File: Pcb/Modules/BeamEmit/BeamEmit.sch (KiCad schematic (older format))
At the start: 15 parts, among them J1 MICRO_USB, Q1 Q_NMOS_GSD, U1 LM555N

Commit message: Update module pcbs
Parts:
- added X1, X2, X3, X4: HOLE, Mounting_Holes:MountingHole_2.5mm_Pad, symbol HOLE
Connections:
- no-connect marks 1 -> 4
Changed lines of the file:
@@
 	7050 4850 7050 5000
 $Comp
-L GND #PWR11
+L GND #PWR01
 U 1 1 59FD7258
 P 7050 5000
-F 0 "#PWR11" H 7050 4750 50  0001 C CNN
+F 0 "#PWR01" H 7050 4750 50  0001 C CNN
 F 1 "GND" H 7050 4850 50  0000 C CNN
 F 2 "" H 7050 5000 50  0000 C CNN
@@
 $EndComp
 $Comp
-L +5V #PWR1
+L +5V #PWR02
 U 1 1 5A21CEBB
 P 3100 4000
-F 0 "#PWR1" H 3100 3850 50  0001 C CNN
+F 0 "#PWR02" H 3100 3850 50  0001 C CNN
 F 1 "+5V" H 3100 4140 50  0000 C CNN
 F 2 "" H 3100 4000 50  0000 C CNN
@@
 $EndComp
 $Comp
-L GND #PWR2
+L GND #PWR03
 U 1 1 5A21D01D
 P 3100 4500
-F 0 "#PWR2" H 3100 4250 50  0001 C CNN
+F 0 "#PWR03" H 3100 4250 50  0001 C CNN
 F 1 "GND" H 3100 4350 50  0000 C CNN
 F 2 "" H 3100 4500 50  0000 C CNN
@@
 $EndComp
 $Comp
-L VCC #PWR3
+L VCC #PWR04
 U 1 1 5A21E1C2
 P 3300 4000
-F 0 "#PWR3" H 3300 3850 50  0001 C CNN
+F 0 "#PWR04" H 3300 3850 50  0001 C CNN
 F 1 "VCC" H 3300 4150 50  0000 C CNN
 F 2 "" H 3300 4000 50  0000 C CNN
@@
 	4700 4200 4850 4200
 $Comp
-L +5V #PWR6
+L +5V #PWR05
 U 1 1 5A21EBAD
 P 4700 4200
-F 0 "#PWR6" H 4700 4050 50  0001 C CNN
+F 0 "#PWR05" H 4700 4050 50  0001 C CNN
 F 1 "+5V" H 4700 4340 50  0000 C CNN
 F 2 "" H 4700 4200 50  0000 C CNN
@@
 $EndComp
 $Comp
-L GND #PWR4
+L GND #PWR06
 U 1 1 5A21EE4C
 P 4400 4350
-F 0 "#PWR4" H 4400 4100 50  0001 C CNN
+F 0 "#PWR06" H 4400 4100 50  0001 C CNN
 F 1 "GND" H 4400 4200 50  0000 C CNN
 F 2 "" H 4400 4350 50  0000 C CNN
@@
 Connection ~ 5550 4700
 $Comp
-L GND #PWR7
+L GND #PWR07
 U 1 1 5A21F0BA
 P 5550 5000
-F 0 "#PWR7" H 5550 4750 50  0001 C CNN
+F 0 "#PWR07" H 5550 4750 50  0001 C CNN
 F 1 "GND" H 5550 4850 50  0000 C CNN
 F 2 "" H 5550 5000 50  0000 C CNN
@@
 	4400 4000 4850 4000
 $Comp
-L +5V #PWR5
+L +5V #PWR08
 U 1 1 5A21F5D3
 P 4550 3400
-F 0 "#PWR5" H 4550 3250 50  0001 C CNN
+F 0 "#PWR08" H 4550 3250 50  0001 C CNN
 F 1 "+5V" H 4550 3540 50  0000 C CNN
 F 2 "" H 4550 3400 50  0000 C CNN
@@
 $EndComp
 $Comp
-L +5V #PWR8
+L +5V #PWR09
 U 1 1 5A21FBAE
 P 6100 3150
-F 0 "#PWR8" H 6100 3000 50  0001 C CNN
+F 0 "#PWR09" H 6100 3000 50  0001 C CNN
 F 1 "+5V" H 6100 3290 50  0000 C CNN
 F 2 "" H 6100 3150 50  0000 C CNN
@@
 $EndComp
 $Comp
-L GND #PWR9
+L GND #PWR010
 U 1 1 5A21FBE3
 P 6100 3350
-F 0 "#PWR9" H 6100 3100 50  0001 C CNN
+F 0 "#PWR010" H 6100 3100 50  0001 C CNN
 F 1 "GND" H 6100 3200 50  0000 C CNN
 F 2 "" H 6100 3350 50  0000 C CNN
@@
 $EndComp
 $Comp
-L +5V #PWR10
+L +5V #PWR011
 U 1 1 5A220329
 P 7050 3400
-F 0 "#PWR10" H 7050 3250 50  0001 C CNN
+F 0 "#PWR011" H 7050 3250 50  0001 C CNN
 F 1 "+5V" H 7050 3540 50  0000 C CNN
 F 2 "" H 7050 3400 50  0000 C CNN
@@
 Text Notes 4300 2800 0    60   ~ 0
 f = 1 / (0.693 * (2*(R3+R5) * C4)
+$Comp
+L HOLE X1
+U 1 1 5A22D73E
+P 4050 5500
+F 0 "X1" H 4050 5400 60  0000 C CNN
+F 1 "HOLE" H 4050 5600 60  0000 C CNN
+F 2 "Mounting_Holes:MountingHole_2.5mm_Pad" H 4050 5500 60  0001 C CNN
+F 3 "" H 4050 5500 60  0000 C CNN
+	1    4050 5500
+	1    0    0    -1
+$EndComp
+$Comp
+L HOLE X2
+U 1 1 5A22E2CB
+P 4350 5500
+F 0 "X2" H 4350 5400 60  0000 C CNN
+F 1 "HOLE" H 4350 5600 60  0000 C CNN
+F 2 "Mounting_Holes:MountingHole_2.5mm_Pad" H 4350 5500 60  0001 C CNN
+F 3 "" H 4350 5500 60  0000 C CNN
+	1    4350 5500
+	1    0    0    -1
+$EndComp
+$Comp
+L HOLE X3
+U 1 1 5A22E316
+P 4650 5500
+F 0 "X3" H 4650 5400 60  0000 C CNN
+F 1 "HOLE" H 4650 5600 60  0000 C CNN
+F 2 "Mounting_Holes:MountingHole_2.5mm_Pad" H 4650 5500 60  0001 C CNN
+F 3 "" H 4650 5500 60  0000 C CNN
+	1    4650 5500
+	1    0    0    -1
+$EndComp
+$Comp
+L HOLE X4
+U 1 1 5A22E364
+P 4950 5500
+F 0 "X4" H 4950 5400 60  0000 C CNN
+F 1 "HOLE" H 4950 5600 60  0000 C CNN
+F 2 "Mounting_Holes:MountingHole_2.5mm_Pad" H 4950 5500 60  0001 C CNN
+F 3 "" H 4950 5500 60  0000 C CNN
+	1    4950 5500
+	1    0    0    -1
+$EndComp
+NoConn ~ 2900 4150
+NoConn ~ 2900 4250
+NoConn ~ 2900 4350
 $EndSCHEMATC

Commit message: Update beam emitter to use single 20k
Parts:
- removed R5: 10K, Resistors_SMD:R_0603, symbol R
- R3: value 10K -> 20K
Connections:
- net at R4.1, U1.3 (Q): now also R3.2
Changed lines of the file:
@@
 P 5150 3400
 F 0 "R3" V 5230 3400 50  0000 C CNN
-F 1 "10K" V 5150 3400 50  0000 C CNN
+F 1 "20K" V 5150 3400 50  0000 C CNN
 F 2 "Resistors_SMD:R_0603" V 5080 3400 50  0001 C CNN
 F 3 "" H 5150 3400 50  0001 C CNN
 	1    5150 3400
-	0    -1   -1   0
-$EndComp
-$Comp
-L R R5
-U 1 1 5A21E86F
-P 5650 3400
-F 0 "R5" V 5730 3400 50  0000 C CNN
-F 1 "10K" V 5650 3400 50  0000 C CNN
-F 2 "Resistors_SMD:R_0603" V 5580 3400 50  0001 C CNN
-F 3 "" H 5650 3400 50  0001 C CNN
-	1    5650 3400
 	0    -1   -1   0
 $EndComp
@@
 	4800 3400 5000 3400
 Wire Wire Line
-	5800 3400 5900 3400
+	5300 3400 5900 3400
 Wire Wire Line
 	5900 3400 5900 3800
 Wire Wire Line
-	5500 3400 5300 3400
-Wire Wire Line
 	4700 4200 4850 4200

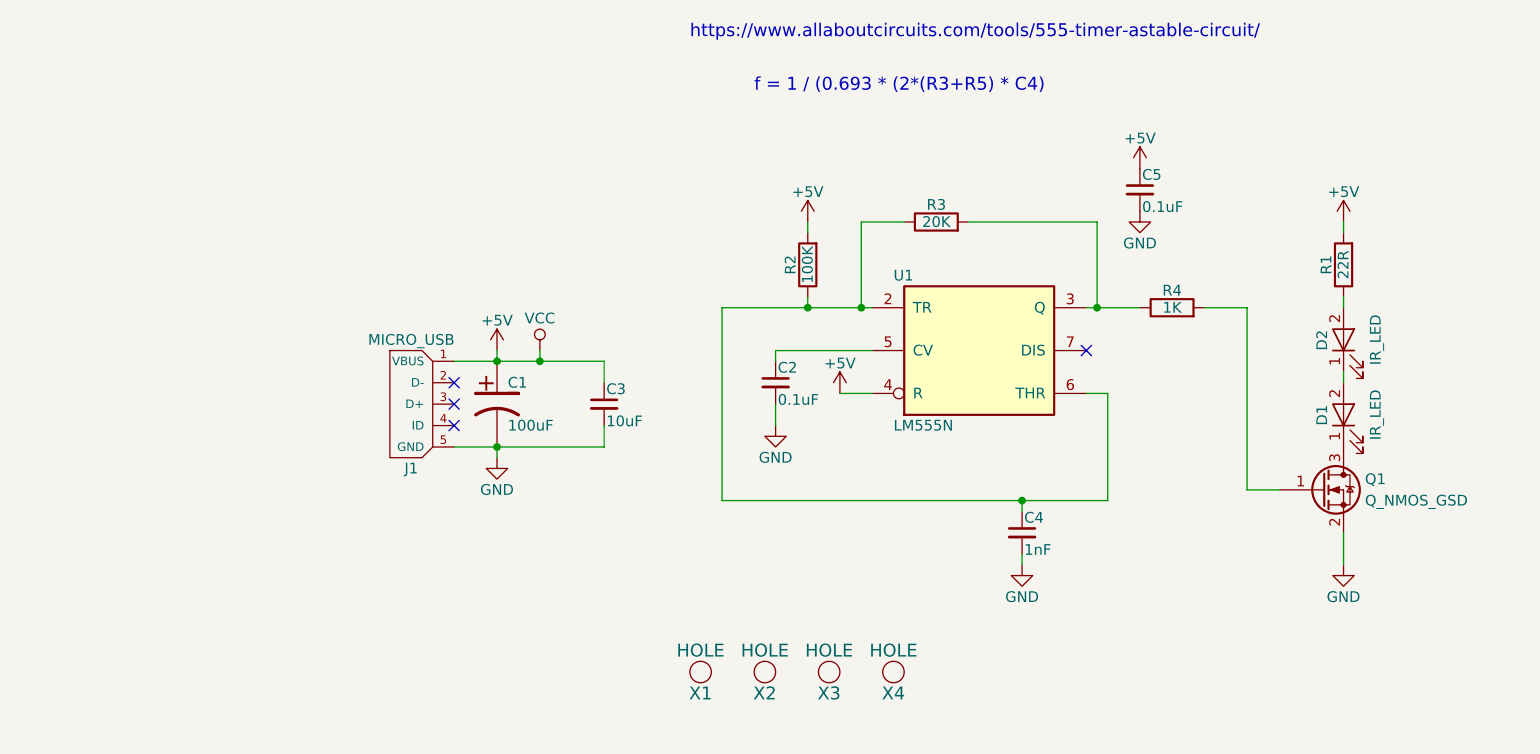
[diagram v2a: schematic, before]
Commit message: Update module pcbs
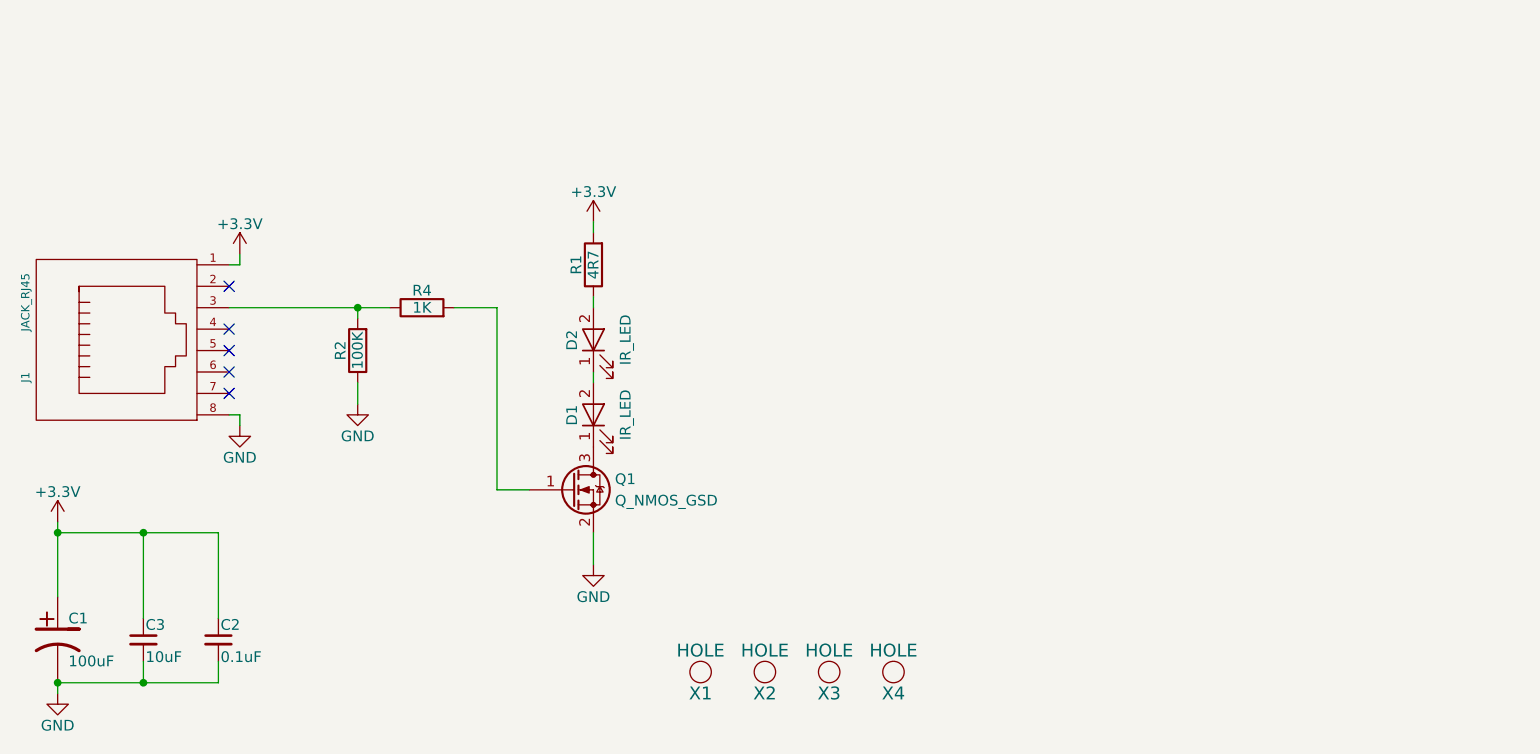
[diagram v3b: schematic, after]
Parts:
- removed C4: 1nF, Capacitors_SMD:C_0603, symbol C_Small
- removed C5: 0.1uF, Capacitors_SMD:C_0603, symbol C_Small
- removed J1: MICRO_USB, CA6:USB_MICRO_10118194-0001LF, symbol MICRO_USB
- removed R3: 20K, Resistors_SMD:R_0603, symbol R
- removed U1: LM555N, SMD_Packages:SOIC-8-N, symbol LM555N
- added J1: JACK_RJ45, CA6:RJ45_pcbwing, symbol JACK_RJ45
- R1: value 22R -> 4R7
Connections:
- net GND: now also R2.1, J1.8
- net at R4.1: now also R2.2, J1.3
- net +3V3: now reaches C2.1
- net +3V3: now also C1.1, C3.1, R1.2, J1.1
- removed net +5V: C1.1, C3.1, R1.2, R2.2
- no-connect marks 4 -> 5
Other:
- note removed: "f = 1 / (0.693 * (2*(R3+R5) * C4)"
- note removed: "https://www.allaboutcircuits.com/tools/555-timer-astable-circuit/"
- moved on the sheet: C1, C2, C3, D1, D2, Q1, R1, R2, R4

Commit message: Update pcb for new switch
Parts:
- C1: symbol CAP_ELEC -> CA6:CAP_ELEC
- C2, C3: symbol C_Small -> Device:C_Small
- D1, D2: symbol LED -> Device:LED
- J1: symbol JACK_RJ45 -> CA6:JACK_RJ45
- Q1: symbol Q_NMOS_GSD -> Device:Q_NMOS_GSD
- R1, R2, R4: symbol R -> Device:R
- X1, X2, X3, X4: symbol HOLE -> CA6:HOLE
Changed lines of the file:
@@
-EESchema Schematic File Version 2
-LIBS:power
-LIBS:device
-LIBS:switches
-LIBS:relays
-LIBS:motors
-LIBS:transistors
-LIBS:conn
-LIBS:linear
-LIBS:regul
-LIBS:74xx
-LIBS:cmos4000
-LIBS:adc-dac
-LIBS:memory
-LIBS:xilinx
-LIBS:microcontrollers
-LIBS:dsp
-LIBS:microchip
-LIBS:analog_switches
-LIBS:motorola
-LIBS:texas
-LIBS:intel
-LIBS:audio
-LIBS:interface
-LIBS:digital-audio
-LIBS:philips
-LIBS:display
-LIBS:cypress
-LIBS:siliconi
-LIBS:opto
-LIBS:atmel
-LIBS:contrib
-LIBS:valves
-LIBS:CA6
+EESchema Schematic File Version 4
 LIBS:BeamEmit-cache
-EELAYER 25 0
+EELAYER 26 0
 EELAYER END
 $Descr A4 11693 8268
@@
 $EndDescr
 $Comp
-L C_Small C3
+L Device:C_Small C3
 U 1 1 59FF8067
 P 1450 5350
@@
 $EndComp
 $Comp
-L GND #PWR01
+L power:GND #PWR01
 U 1 1 5A21D01D
 P 1050 5600
@@
 $EndComp
 $Comp
-L CAP_ELEC C1
+L CA6:CAP_ELEC C1
 U 1 1 5A21D205
 P 1050 5350
@@
 $EndComp
 $Comp
-L R R2
+L Device:R R2
 U 1 1 5A21EBE0
 P 2450 4000
@@
 $EndComp
 $Comp
-L C_Small C2
+L Device:C_Small C2
 U 1 1 5A21ED48
 P 1800 5350
@@
 $EndComp
 $Comp
-L HOLE X1
+L CA6:HOLE X1
 U 1 1 5A22D73E
 P 4050 5500
@@
 $EndComp
 $Comp
-L HOLE X2
+L CA6:HOLE X2
 U 1 1 5A22E2CB
 P 4350 5500
@@
 $EndComp
 $Comp
-L HOLE X3
+L CA6:HOLE X3
 U 1 1 5A22E316
 P 4650 5500
@@
 $EndComp
 $Comp
-L HOLE X4
+L CA6:HOLE X4
 U 1 1 5A22E364
 P 4950 5500
@@
 $EndComp
 $Comp
-L JACK_RJ45 J1
+L CA6:JACK_RJ45 J1
 U 1 1 5ABE5A75
 P 1400 3950
@@
 $EndComp
 $Comp
-L +3.3V #PWR02
+L power:+3.3V #PWR02
 U 1 1 5ABE5EDB
 P 1050 4800
@@
 $EndComp
 $Comp
-L GND #PWR03
+L power:GND #PWR03
 U 1 1 59FD7258
 P 3550 5000
@@
 $EndComp
 $Comp
-L R R1
+L Device:R R1
 U 1 1 59FD89F4
 P 3550 3600
@@
 $EndComp
 $Comp
-L LED D2
+L Device:LED D2
 U 1 1 5A221E37
 P 3550 3950
@@
 $EndComp
 $Comp
-L LED D1
+L Device:LED D1
 U 1 1 59CD43E5
 P 3550 4300
@@
 $EndComp
 $Comp
-L Q_NMOS_GSD Q1
+L Device:Q_NMOS_GSD Q1
 U 1 1 59FD80EC
 P 3450 4650
@@
 $EndComp
 $Comp
-L R R4
+L Device:R R4
 U 1 1 59D0E70C
 P 2750 3800
@@
 Connection ~ 1450 4850
 Wire Wire Line
-	1050 4800 1050 5150
+	1050 4800 1050 4850
 Connection ~ 1050 4850
 Wire Wire Line
-	1050 4850 1800 4850
-Wire Wire Line
-	1050 5550 1800 5550
-$Comp
-L +3.3V #PWR05
+	1050 4850 1450 4850
+Wire Wire Line
+	1050 5550 1450 5550
+$Comp
+L power:+3.3V #PWR05
 U 1 1 5ABE7EAD
 P 1900 3550
@@
 $EndComp
 $Comp
-L GND #PWR06
+L power:GND #PWR06
 U 1 1 5ABE7EE2
 P 1900 4350
@@
 	1900 4300 1900 4350
 $Comp
-L GND #PWR07
+L power:GND #PWR07
 U 1 1 5ABE81CF
 P 2450 4250
@@
 $EndComp
 Wire Wire Line
-	1850 3800 2600 3800
+	1850 3800 2450 3800
 Wire Wire Line
 	2450 3850 2450 3800
@@
 NoConn ~ 1850 4200
 $Comp
-L +3.3V #PWR?
+L power:+3.3V #PWR?
 U 1 1 5ABE5DD5
 P 3550 3400
@@
 	1    0    0    -1
 $EndComp
+Wire Wire Line
+	1450 5550 1800 5550
+Wire Wire Line
+	1450 4850 1800 4850
+Wire Wire Line
+	1050 4850 1050 5150
+Wire Wire Line
+	2450 3800 2600 3800
 $EndSCHEMATC
